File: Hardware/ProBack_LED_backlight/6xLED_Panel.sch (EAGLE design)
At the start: 17 parts

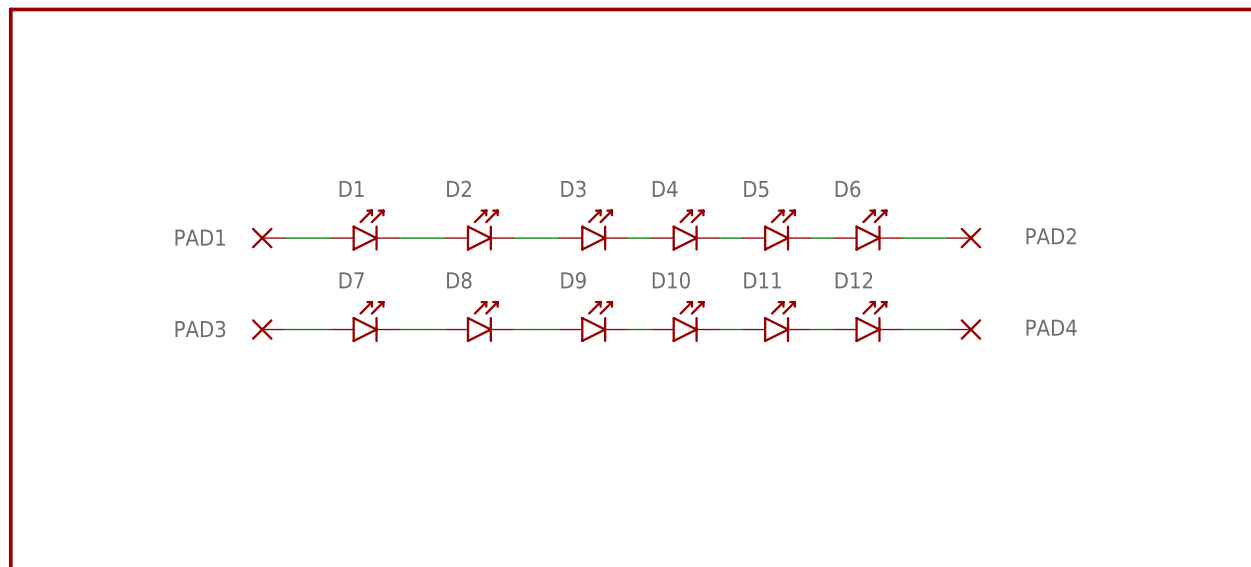
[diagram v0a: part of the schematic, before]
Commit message: Updated for PCBWay of doing boards
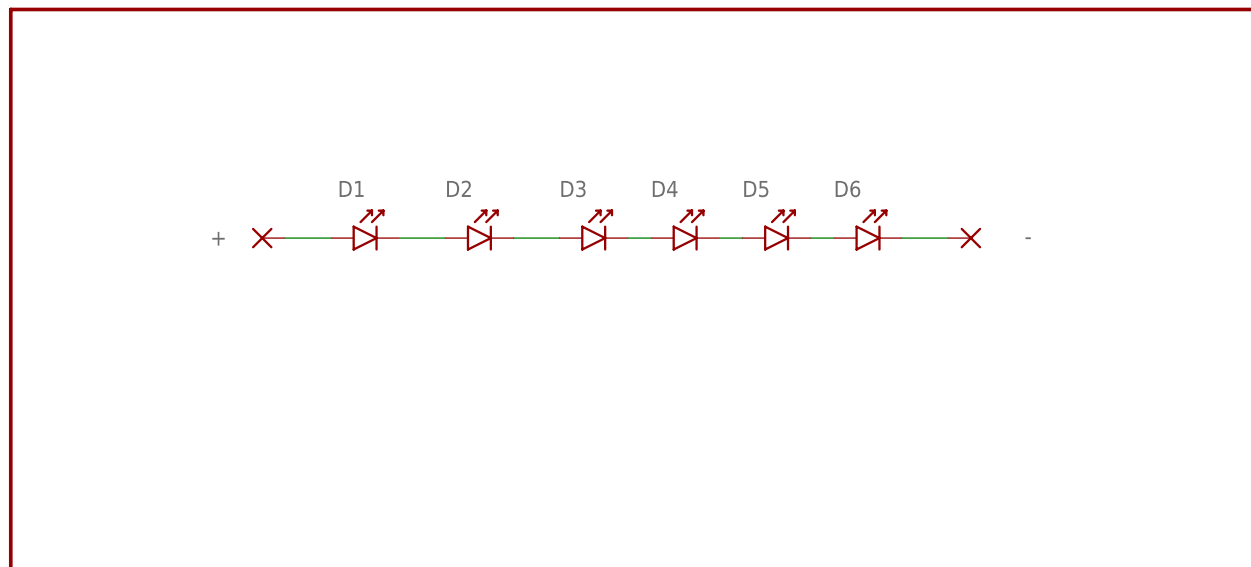
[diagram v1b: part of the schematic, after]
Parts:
- removed D10, D11, D12, D7, D8, D9: YUJI_2835_SMD, Yuji_LED:YUJI_2835_SMD
- removed PAD3: WIREPAD1,6/0,9, wirepad:2,15/1,0
- removed PAD4: (no value), wirepad:2,15/1,0
- renumbered PAD1 to +, PAD2 to -
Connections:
- removed net N$12: D10.ANODE, D9.CATHODE
- removed net N$13: D10.CATHODE, D11.ANODE
- removed net N$14: D11.CATHODE, D12.ANODE
- removed net N$5: D7.CATHODE, D8.ANODE
- removed net N$6: D7.ANODE, PAD3.P
- removed net N$7: D8.CATHODE, D9.ANODE
- removed net N$8: D12.CATHODE, PAD4.P
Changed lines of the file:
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@@
 <attribute name="VER" value="1.0"/>
 </part>
-<part name="PAD1" library="wirepad" deviceset="2,15/1,0" device="" package3d_urn="urn:adsk.eagle:package:30831/1" value="WIREPAD1,6/0,9"/>
-<part name="PAD2" library="wirepad" deviceset="2,15/1,0" device="" package3d_urn="urn:adsk.eagle:package:30831/1"/>
+<part name="+" library="wirepad" deviceset="2,15/1,0" device="" package3d_urn="urn:adsk.eagle:package:30831/1" value="WIREPAD1,6/0,9"/>
+<part name="-" library="wirepad" deviceset="2,15/1,0" device="" package3d_urn="urn:adsk.eagle:package:30831/1"/>
 <part name="D3" library="Yuji_LED" deviceset="YUJI_2835_SMD" device=""/>
-<part name="D7" library="Yuji_LED" deviceset="YUJI_2835_SMD" device=""/>
-<part name="D8" library="Yuji_LED" deviceset="YUJI_2835_SMD" device=""/>
-<part name="PAD3" library="wirepad" deviceset="2,15/1,0" device="" package3d_urn="urn:adsk.eagle:package:30831/1" value="WIREPAD1,6/0,9"/>
-<part name="PAD4" library="wirepad" deviceset="2,15/1,0" device="" package3d_urn="urn:adsk.eagle:package:30831/1"/>
-<part name="D9" library="Yuji_LED" deviceset="YUJI_2835_SMD" device=""/>
 <part name="D4" library="Yuji_LED" deviceset="YUJI_2835_SMD" device=""/>
 <part name="D5" library="Yuji_LED" deviceset="YUJI_2835_SMD" device=""/>
 <part name="D6" library="Yuji_LED" deviceset="YUJI_2835_SMD" device=""/>
-<part name="D10" library="Yuji_LED" deviceset="YUJI_2835_SMD" device=""/>
-<part name="D11" library="Yuji_LED" deviceset="YUJI_2835_SMD" device=""/>
-<part name="D12" library="Yuji_LED" deviceset="YUJI_2835_SMD" device=""/>
 </parts>
 <sheets>
@@
 </instance>
 <instance part="FRAME1" gate="G$1" x="0" y="0" smashed="yes"/>
-<instance part="PAD1" gate="1" x="27.94" y="96.52" smashed="yes">
+<instance part="+" gate="1" x="27.94" y="96.52" smashed="yes">
 <attribute name="NAME" x="24.003" y="97.4598" size="1.778" layer="95" rot="R180"/>
 </instance>
-<instance part="PAD2" gate="1" x="106.68" y="96.52" smashed="yes" rot="R180">
+<instance part="-" gate="1" x="106.68" y="96.52" smashed="yes" rot="R180">
 <attribute name="NAME" x="112.649" y="95.8342" size="1.778" layer="95"/>
 <attribute name="VALUE" x="107.823" y="99.822" size="1.778" layer="96" rot="R180"/>
@@
 <instance part="D3" gate="G$1" x="66.04" y="96.52" smashed="yes">
 <attribute name="NAME" x="60.96" y="101.092" size="1.778" layer="95"/>
-</instance>
-<instance part="D7" gate="G$1" x="40.64" y="86.36" smashed="yes">
-<attribute name="NAME" x="36.322" y="90.932" size="1.778" layer="95"/>
-</instance>
-<instance part="D8" gate="G$1" x="53.34" y="86.36" smashed="yes">
-<attribute name="NAME" x="48.26" y="90.932" size="1.778" layer="95"/>
-</instance>
-<instance part="PAD3" gate="1" x="27.94" y="86.36" smashed="yes">
-<attribute name="NAME" x="24.003" y="87.2998" size="1.778" layer="95" rot="R180"/>
-</instance>
-<instance part="PAD4" gate="1" x="106.68" y="86.36" smashed="yes" rot="R180">
-<attribute name="NAME" x="112.649" y="85.6742" size="1.778" layer="95"/>
-<attribute name="VALUE" x="107.823" y="89.662" size="1.778" layer="96" rot="R180"/>
-</instance>
-<instance part="D9" gate="G$1" x="66.04" y="86.36" smashed="yes">
-<attribute name="NAME" x="60.96" y="90.932" size="1.778" layer="95"/>
 </instance>
 <instance part="D4" gate="G$1" x="76.2" y="96.52" smashed="yes">
@@
 <instance part="D6" gate="G$1" x="96.52" y="96.52" smashed="yes">
 <attribute name="NAME" x="91.44" y="101.092" size="1.778" layer="95"/>
-</instance>
-<instance part="D10" gate="G$1" x="76.2" y="86.36" smashed="yes">
-<attribute name="NAME" x="71.12" y="90.932" size="1.778" layer="95"/>
-</instance>
-<instance part="D11" gate="G$1" x="86.36" y="86.36" smashed="yes">
-<attribute name="NAME" x="81.28" y="90.932" size="1.778" layer="95"/>
-</instance>
-<instance part="D12" gate="G$1" x="96.52" y="86.36" smashed="yes">
-<attribute name="NAME" x="91.44" y="90.932" size="1.778" layer="95"/>
 </instance>
 </instances>
@@
 <net name="N$2" class="0">
 <segment>
-<pinref part="PAD1" gate="1" pin="P"/>
+<pinref part="+" gate="1" pin="P"/>
 <pinref part="D1" gate="G$1" pin="ANODE"/>
 <wire x1="30.48" y1="96.52" x2="35.56" y2="96.52" width="0.1524" layer="91"/>
@@
 <net name="N$4" class="0">
 <segment>
-<pinref part="PAD2" gate="1" pin="P"/>
+<pinref part="-" gate="1" pin="P"/>
 <wire x1="99.06" y1="96.52" x2="104.14" y2="96.52" width="0.1524" layer="91"/>
 <pinref part="D6" gate="G$1" pin="CATHODE"/>
-</segment>
-</net>
-<net name="N$5" class="0">
-<segment>
-<pinref part="D7" gate="G$1" pin="CATHODE"/>
-<pinref part="D8" gate="G$1" pin="ANODE"/>
-<wire x1="43.18" y1="86.36" x2="48.26" y2="86.36" width="0.1524" layer="91"/>
-</segment>
-</net>
-<net name="N$6" class="0">
-<segment>
-<pinref part="PAD3" gate="1" pin="P"/>
-<pinref part="D7" gate="G$1" pin="ANODE"/>
-<wire x1="30.48" y1="86.36" x2="35.56" y2="86.36" width="0.1524" layer="91"/>
-</segment>
-</net>
-<net name="N$7" class="0">
-<segment>
-<pinref part="D8" gate="G$1" pin="CATHODE"/>
-<pinref part="D9" gate="G$1" pin="ANODE"/>
-<wire x1="55.88" y1="86.36" x2="60.96" y2="86.36" width="0.1524" layer="91"/>
-</segment>
-</net>
-<net name="N$8" class="0">
-<segment>
-<pinref part="PAD4" gate="1" pin="P"/>
-<wire x1="99.06" y1="86.36" x2="104.14" y2="86.36" width="0.1524" layer="91"/>
-<pinref part="D12" gate="G$1" pin="CATHODE"/>
 </segment>
 </net>
@@
 </segment>
 </net>
-<net name="N$12" class="0">
-<segment>
-<pinref part="D9" gate="G$1" pin="CATHODE"/>
-<wire x1="68.58" y1="86.36" x2="71.12" y2="86.36" width="0.1524" layer="91"/>
-<pinref part="D10" gate="G$1" pin="ANODE"/>
-</segment>
-</net>
-<net name="N$13" class="0">
-<segment>
-<pinref part="D10" gate="G$1" pin="CATHODE"/>
-<wire x1="78.74" y1="86.36" x2="81.28" y2="86.36" width="0.1524" layer="91"/>
-<pinref part="D11" gate="G$1" pin="ANODE"/>
-</segment>
-</net>
-<net name="N$14" class="0">
-<segment>
-<pinref part="D11" gate="G$1" pin="CATHODE"/>
-<wire x1="88.9" y1="86.36" x2="91.44" y2="86.36" width="0.1524" layer="91"/>
-<pinref part="D12" gate="G$1" pin="ANODE"/>
-</segment>
-</net>
